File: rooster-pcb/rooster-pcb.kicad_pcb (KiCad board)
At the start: 2 copper layers, 216 x 68 mm, 108 parts, among them M1 MountingHole_2.2mm_M2_Pad, M2 MountingHole_2.2mm_M2_Pad, M3 MountingHole_2.2mm_M2_Pad, M4 MountingHole_2.2mm_M2_Pad, M5 MountingHole_2.2mm_M2_Pad, M6 MountingHole_2.2mm_M2_Pad, M7 MountingHole_2.2mm_M2_Pad, M8 MountingHole_2.2mm_M2_Pad, M9 MountingHole_2.2mm_M2_Pad, SW0-0 SW_Push, SW0-1 SW_Push, SW0-10 SW_Push, SW0-11 SW_Push, SW0-2 SW_Push, SW0-3 SW_Push, SW0-4 SW_Push, SW0-5 SW_Push, SW0-6 SW_Push, SW0-7 SW_Push, SW0-8 SW_Push, SW0-9 SW_Push, SW1-0 SW_Push, SW1-1 SW_Push, SW1-10 SW_Push, SW1-11 SW_Push, SW1-2 SW_Push, SW1-3 SW_Push, SW1-4 SW_Push, SW1-5 SW_Push, SW1-6 SW_Push, SW1-7 SW_Push, SW1-8 SW_Push, SW1-9 SW_Push, SW2-0 SW_Push, SW2-1 SW_Push, SW2-10 SW_Push, SW2-11 SW_Push, SW2-2 SW_Push, SW2-3 SW_Push, SW2-4 SW_Push, SW2-5 SW_Push, SW2-6 SW_Push, SW2-7 SW_Push, SW2-8 SW_Push, SW2-9 SW_Push, SW3-0 SW_Push, SW3-1 SW_Push, SW3-10 SW_Push, SW3-11 SW_Push, SW3-2 SW_Push, SW3-3 SW_Push, SW3-4 SW_Push, SW3-5 SW_Push, SW3-7 SW_Push, SW3-8 SW_Push, SW3-9 SW_Push, U1 ProMicro

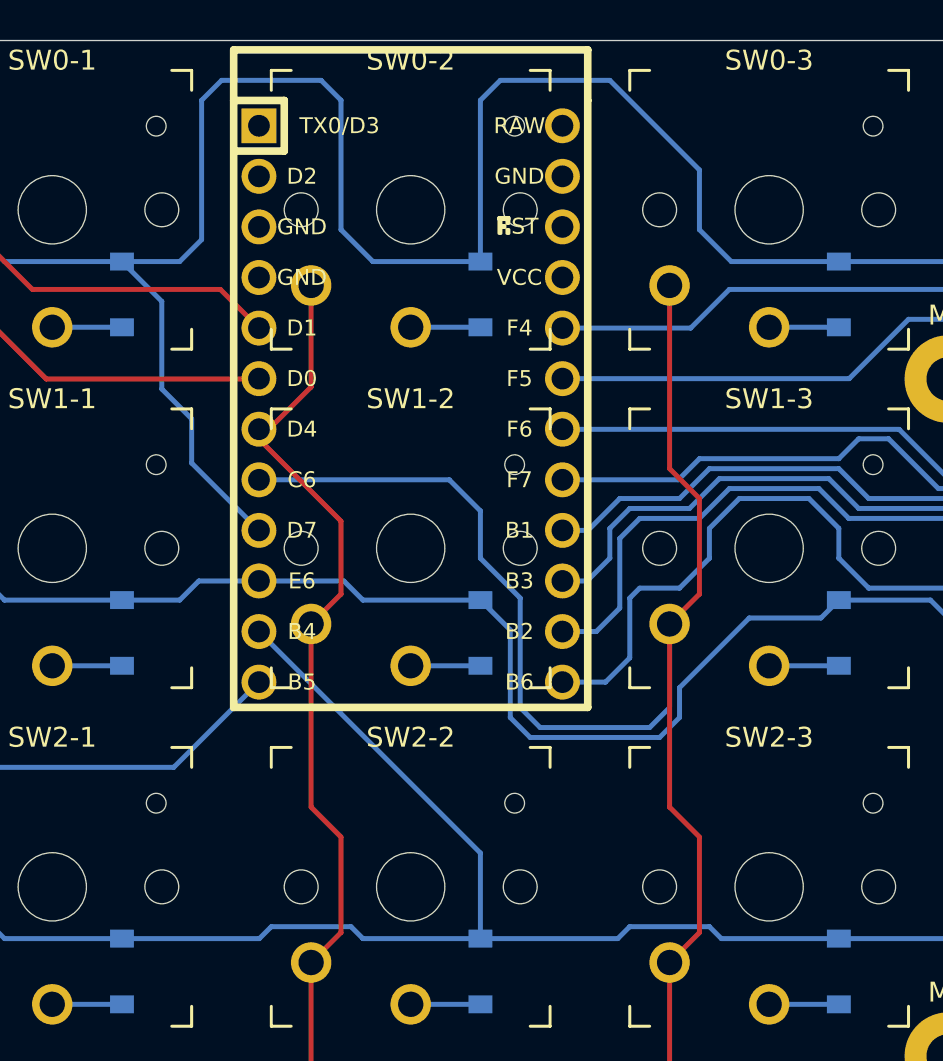
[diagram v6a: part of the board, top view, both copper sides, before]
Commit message: Added Rooster graphics
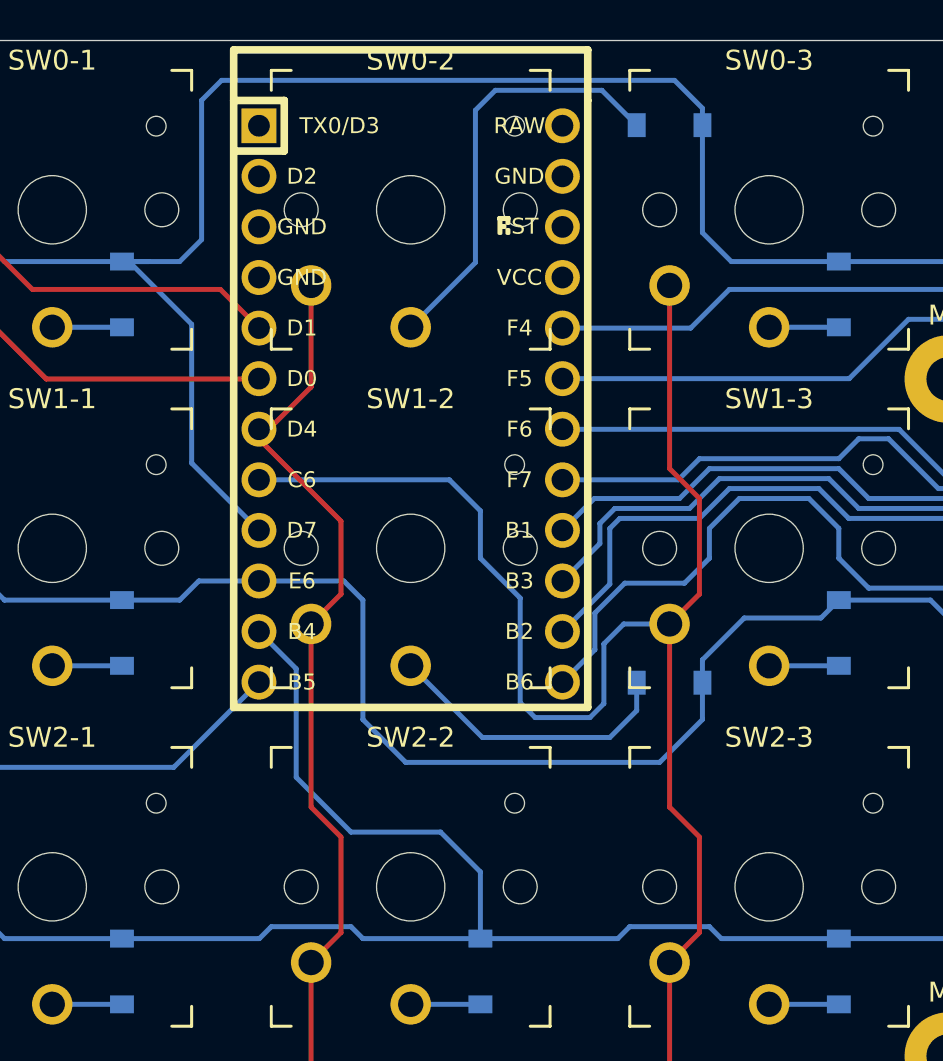
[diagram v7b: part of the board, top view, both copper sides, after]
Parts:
- moved D0-2 12.7 mm to (91.0, 37.8), turned to 180 degrees
- moved D1-2 9.82 mm to (91.0, 65.8), turned to 180 degrees
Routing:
- net Net-(D0-2-Pad2): track 3.50 -> 21.5 mm
- net ROW0: track 248.3 -> 235.7 mm
- net Net-(D1-2-Pad2): track 3.50 -> 14.8 mm
- net ROW1: track 231.0 -> 233.8 mm
- net ROW2: track 223.5 -> 226.1 mm
- net COL3: track 89.7 -> 88.5 mm
- net COL4: track 88.1 -> 87.4 mm
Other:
- board text added: "Rooster v1.0 - https://github.com/timmolderez/rooster-kb"

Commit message: Rooster v1.0 gerbers ready for manufacturing!
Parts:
- added G***: LOGO, Rooster_Graphics:Rooster-front, F.Cu at (222.0, 73.0)
- added G***: LOGO, Rooster_Graphics:Rooster-back, F.Cu at (222.0, 73.0)
